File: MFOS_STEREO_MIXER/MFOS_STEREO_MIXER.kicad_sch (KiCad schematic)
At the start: 0 parts

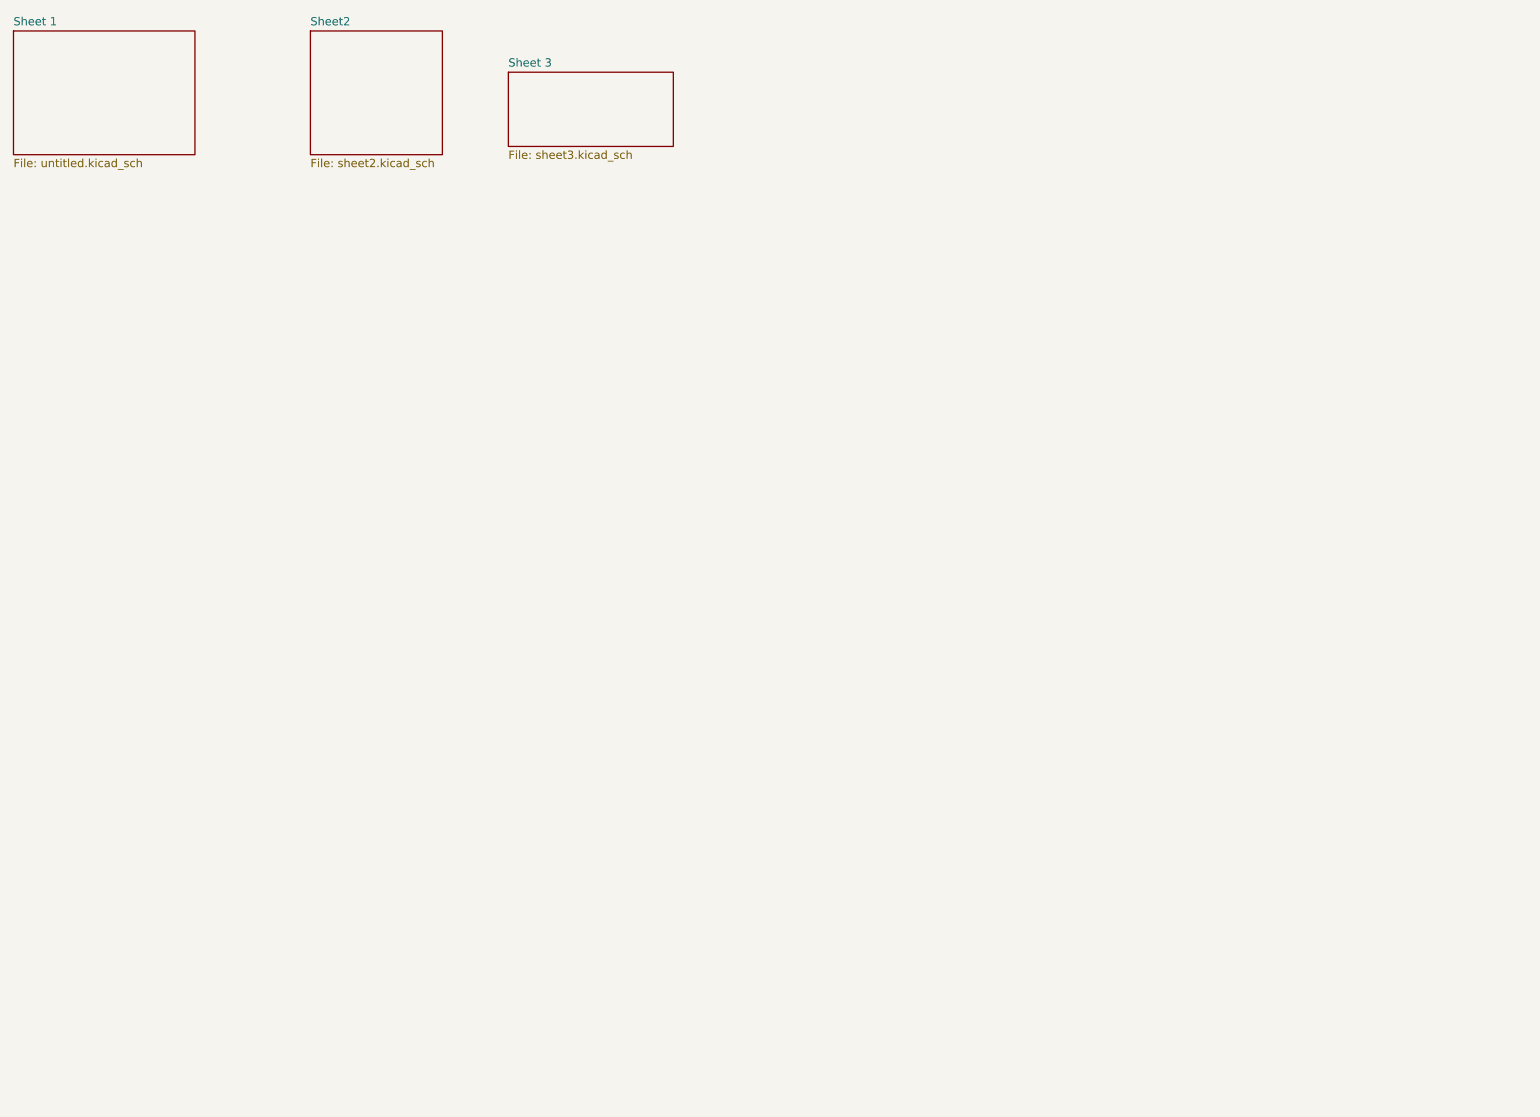
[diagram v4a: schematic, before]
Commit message: Split up design into different sheets
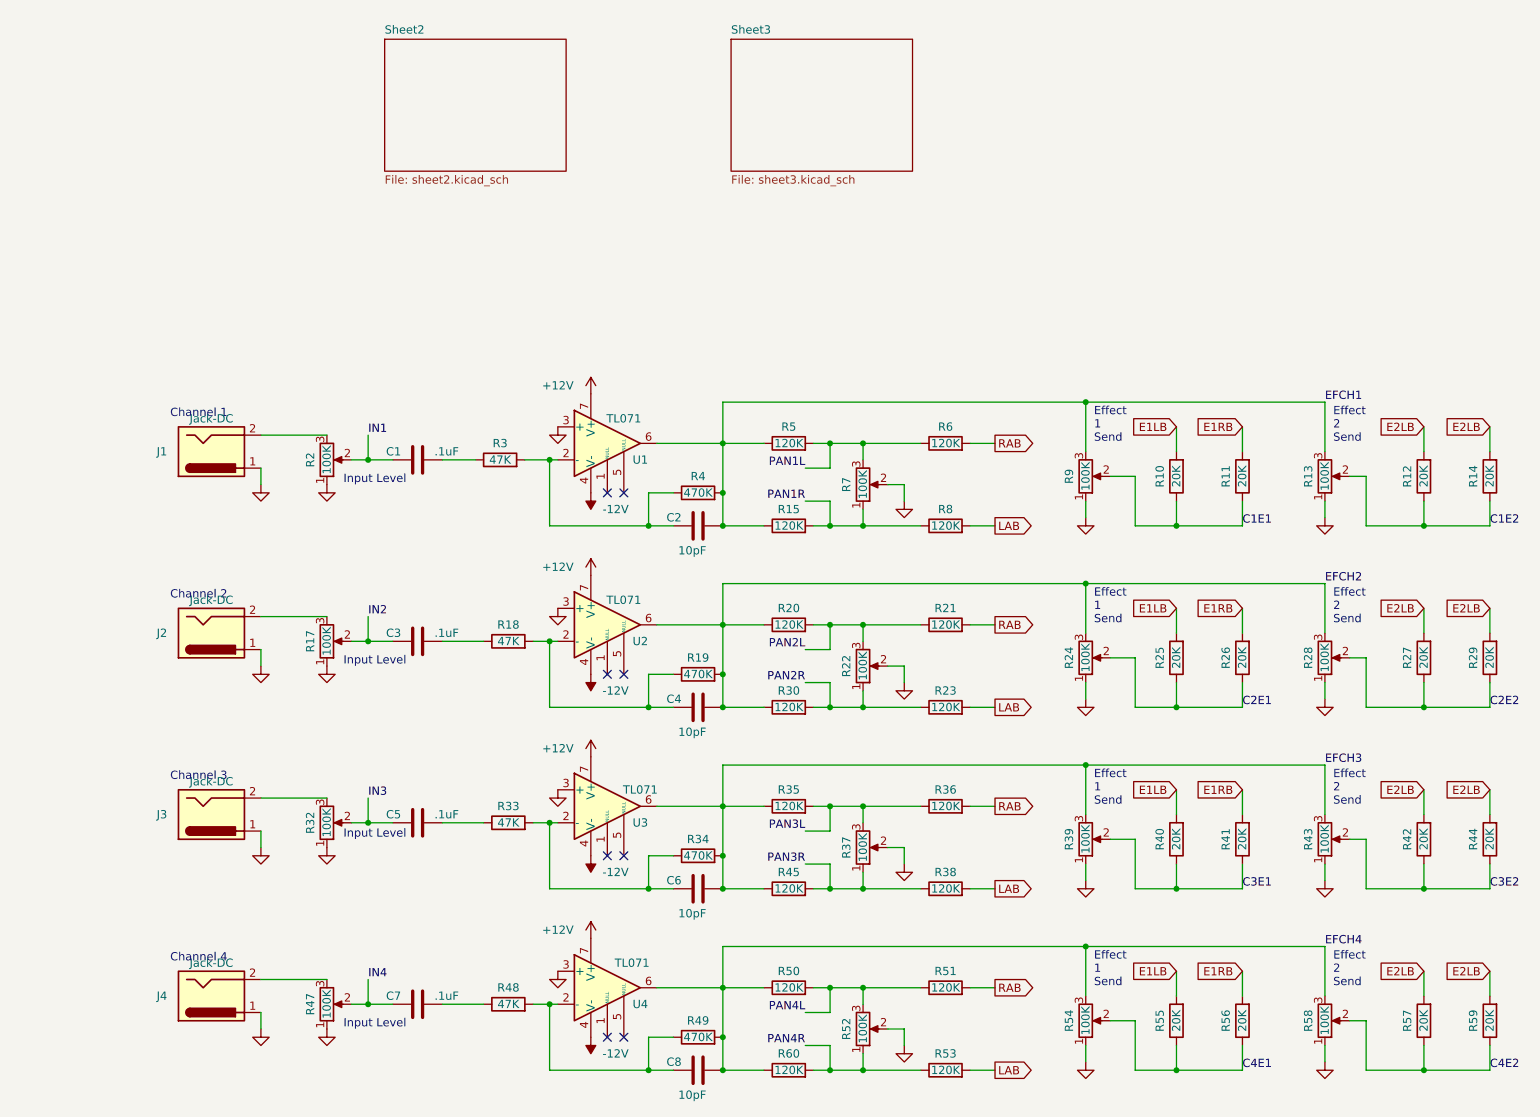
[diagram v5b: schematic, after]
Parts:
- added C1, C3, C5, C7: .1uF, symbol Device:C
- added C2, C4, C6, C8: 10pF, symbol Device:C
- added J1, J2, J3, J4: Jack-DC, symbol Connector:Jack-DC
- added R10, R11, R12, R14, R25, R26, R27, R29, R40, R41, R42, R44, R55, R56, R57, R59: 20K, symbol Device:R
- added R13, R17, R2, R24, R28, R32, R39, R43, R47, R54, R58, R9: 100K, symbol dhk:R_Potentiometer_Audio_Taper
- added R15, R20, R21, R23, R30, R35, R36, R38, R45, R5, R50, R51, R53, R6, R60, R8: 120K, symbol Device:R
- added R18, R3, R33, R48: 47K, symbol Device:R
- added R19, R34, R4, R49: 470K, symbol Device:R
- added R22, R37, R52, R7: 100K, symbol Device:R_Potentiometer
- added U1, U2, U3, U4: TL071, symbol Amplifier_Operational:TL071
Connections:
- new net: C4.1, R18.2, R19.1, U2.2 (-)
- new net: C6.1, R33.2, R34.1, U3.2 (-)
- new net: C8.1, R48.2, R49.1, U4.2 (-)
- new net: C3.2, R18.1
- new net: J4.2, R47.3
- new net: C2.1, R3.2, R4.1, U1.2 (-)
- new net: C1.2, R3.1
- new net: C7.2, R48.1
- new net: J1.2, R2.3
- new net: J2.2, R17.3
- new net: J3.2, R32.3
- new net: C5.2, R33.1
- new net +12V: U1.7 (V+), U2.7 (V+), U3.7 (V+), U4.7 (V+)
- new net -12V: U1.4 (V-), U2.4 (V-), U3.4 (V-), U4.4 (V-)
- new net C1E1: R10.1, R11.1, R9.2
- new net C1E2: R12.1, R13.2, R14.1
- new net C2E1: R24.2, R25.1, R26.1
- new net C2E2: R27.1, R28.2, R29.1
- new net C3E1: R39.2, R40.1, R41.1
- new net C3E2: R42.1, R43.2, R44.1
- new net C4E1: R54.2, R55.1, R56.1
- new net C4E2: R57.1, R58.2, R59.1
- new net E1LB: R10.2, R25.2, R40.2, R55.2
- new net E1RB: R11.2, R26.2, R41.2, R56.2
- new net E2LB: R12.2, R14.2, R27.2, R29.2, R42.2, R44.2, R57.2, R59.2
- new net EFCH1: C2.2, R13.3, R15.1, R4.2, R5.1, R9.3, U1.6
- new net EFCH2: C4.2, R19.2, R20.1, R24.3, R28.3, R30.1, U2.6
- new net EFCH3: C6.2, R34.2, R35.1, R39.3, R43.3, R45.1, U3.6
- new net EFCH4: C8.2, R49.2, R50.1, R54.3, R58.3, R60.1, U4.6
- new net GND: J1.1, J2.1, J3.1, J4.1, R13.1, R17.1, R2.1, R22.2, R24.1, R28.1, R32.1, R37.2, R39.1, R43.1, R47.1, R52.2, R54.1, R58.1, R7.2, R9.1, U1.3 (+), U2.3 (+), U3.3 (+), U4.3 (+)
- new net IN1: C1.1, R2.2
- new net IN2: C3.1, R17.2
- new net IN3: C5.1, R32.2
- new net IN4: C7.1, R47.2
- new net LAB: R23.2, R38.2, R53.2, R8.2
- new net PAN1L: R5.2, R6.1, R7.3
- new net PAN1R: R15.2, R7.1, R8.1
- new net PAN2L: R20.2, R21.1, R22.3
- new net PAN2R: R22.1, R23.1, R30.2
- new net PAN3L: R35.2, R36.1, R37.3
- new net PAN3R: R37.1, R38.1, R45.2
- new net PAN4L: R50.2, R51.1, R52.3
- new net PAN4R: R52.1, R53.1, R60.2
- new net RAB: R21.2, R36.2, R51.2, R6.2
- no-connect marks 0 -> 8
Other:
- removed sheet Sheet 1
- removed sheet Sheet 3
- added sheet Sheet3 (sheet3.kicad_sch)
- note added: "Channel 1"
- note added: "Channel 2"
- note added: "Channel 3"
- note added: "Channel 4"
- note added: "Effect 1 Send"
- note added: "Effect 2 Send"
- note added: "Input Level"
